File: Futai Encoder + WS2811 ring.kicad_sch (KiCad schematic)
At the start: 42 parts, among them J1 Conn_02x05_Top_Bottom, SW1 RotaryEncoder_Switch_RGB

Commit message: v0.9
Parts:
- added R51, R61, R71: 15k, Resistor_SMD:R_0805_2012Metric, symbol Device:R_Small
- added R52, R62, R72: 2k, Resistor_SMD:R_0805_2012Metric, symbol Device:R_Small
- added R81: 100, Resistor_SMD:R_0805_2012Metric, symbol Device:R_Small
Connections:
- net +5VL: now also R81.1; no longer SW1.1 (C+)
- net BLU: now also R71.1, R72.2; no longer J1.8 (Pin_8)
- net GND: now also R52.1, R62.1, R72.1
- net GRE: now also R61.1, R62.2; no longer J1.7 (Pin_7)
- net RED: now also R51.1, R52.2; no longer J1.6 (Pin_6)
- new net: R81.2, SW1.1 (C+)
- new net Q-BLU: J1.8 (Pin_8), R71.2
- new net Q-GRE: J1.7 (Pin_7), R61.2
- new net Q-RED: J1.6 (Pin_6), R51.2
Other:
- note added: "V deviders for encoder LED ** 24V PWM in expected !**"
- moved on the sheet: C1, C11, C21, C3, C31, C41, C5, C7, C9, D1, D10, D11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

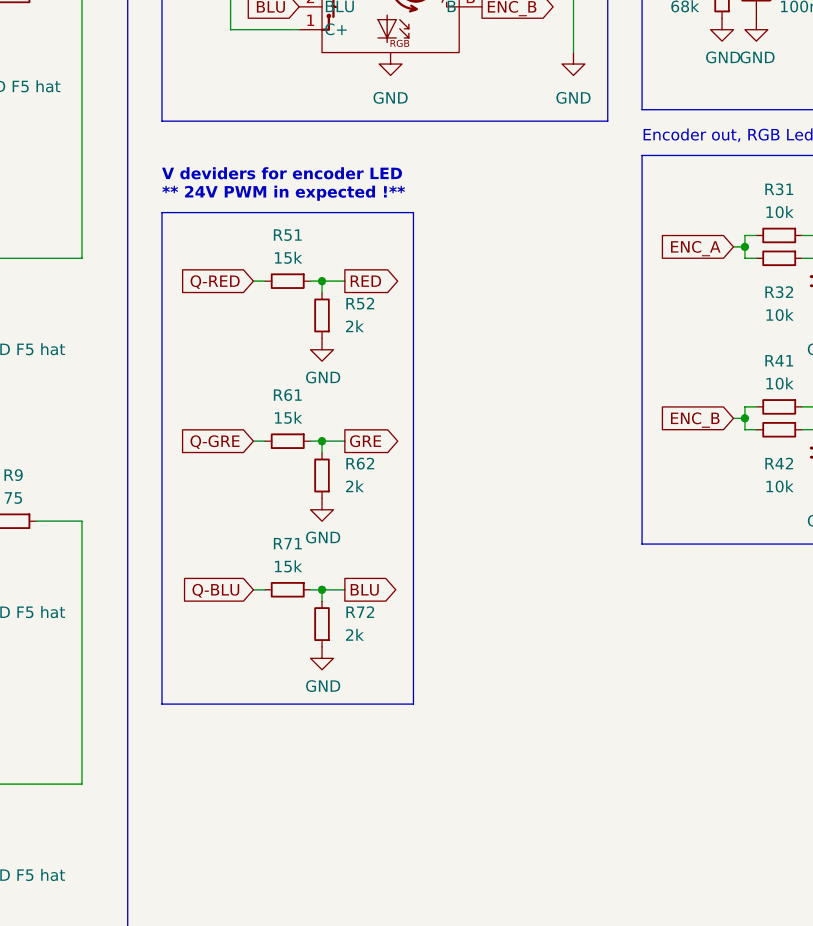
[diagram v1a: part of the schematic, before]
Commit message: better edge cut, adding more info to README.md
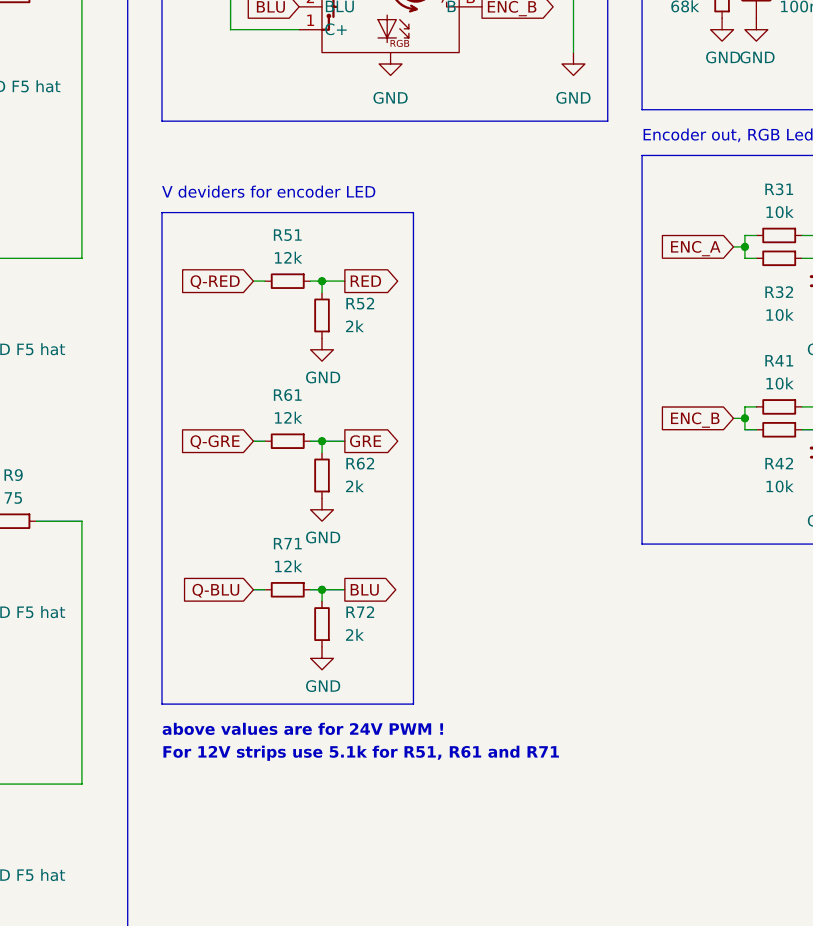
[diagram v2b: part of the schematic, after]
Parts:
- R51, R61, R71: value 15k -> 12k
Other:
- note added: "For 12V strips use 5.1k for R51, R61 and R71"
- note added: "V deviders for encoder LED"
- note added: "above values are for 24V PWM !"
- note removed: "V deviders for encoder LED ** 24V PWM in expected !**"
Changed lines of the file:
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@@
     (stroke (width 0) (type default) (color 0 0 0 0))
+  )
+  (text "For 12V strips use 5.1k for R51, R61 and R71" (at 130.81 134.62 0)
+    (effects (font (size 1.27 1.27) (thickness 0.254) bold) (justify left bottom))
   )
   (text "LED ring" (at 40.64 30.48 0)
@@
     (effects (font (size 1.27 1.27)) (justify left bottom))
   )
+  (text "above values are for 24V PWM !" (at 130.81 132.08 0)
+    (effects (font (size 1.27 1.27) (thickness 0.254) bold) (justify left bottom))
+  )
   (text "Encoder out, RGB Led" (at 184.15 66.04 0)
     (effects (font (size 1.27 1.27)) (justify left bottom))
   )
-  (text "V deviders for encoder LED\n** 24V PWM in expected !**"
-    (at 130.81 72.39 0)
-    (effects (font (size 1.27 1.27) (thickness 0.254) bold) (justify left bottom))
+  (text "V deviders for encoder LED" (at 130.81 72.39 0)
+    (effects (font (size 1.27 1.27)) (justify left bottom))
   )
   (text "Connector interface" (at 274.32 57.15 180)
@@
     (in_bom yes) (on_board yes)
     (property "Reference" "R51" (id 0) (at 144.78 76.2 90))
-    (property "Value" "15k" (id 1) (at 144.78 78.74 90))
+    (property "Value" "12k" (id 1) (at 144.78 78.74 90))
     (property "Footprint" "Resistor_SMD:R_0805_2012Metric" (id 2) (at 144.78 81.28 0)
       (effects (font (size 1.27 1.27)) hide)
@@
     (in_bom yes) (on_board yes)
     (property "Reference" "R61" (id 0) (at 144.78 93.98 90))
-    (property "Value" "15k" (id 1) (at 144.78 96.52 90))
+    (property "Value" "12k" (id 1) (at 144.78 96.52 90))
     (property "Footprint" "Resistor_SMD:R_0805_2012Metric" (id 2) (at 144.78 99.06 0)
       (effects (font (size 1.27 1.27)) hide)
@@
     (in_bom yes) (on_board yes)
     (property "Reference" "R71" (id 0) (at 144.78 110.49 90))
-    (property "Value" "15k" (id 1) (at 144.78 113.03 90))
+    (property "Value" "12k" (id 1) (at 144.78 113.03 90))
     (property "Footprint" "Resistor_SMD:R_0805_2012Metric" (id 2) (at 144.78 115.57 0)
       (effects (font (size 1.27 1.27)) hide)
@@
     )
     (path "/6ff9b25c-f418-4cf8-b38f-8f8fe318f037"
-      (reference "R51") (unit 1) (value "15k") (footprint "Resistor_SMD:R_0805_2012Metric")
+      (reference "R51") (unit 1) (value "12k") (footprint "Resistor_SMD:R_0805_2012Metric")
     )
     (path "/875bf8bf-ec74-4bfd-89a5-45076164d4fd"
@@
     )
     (path "/a1e6e2c4-397e-4467-9a6c-eb9cdfe26fd1"
-      (reference "R61") (unit 1) (value "15k") (footprint "Resistor_SMD:R_0805_2012Metric")
+      (reference "R61") (unit 1) (value "12k") (footprint "Resistor_SMD:R_0805_2012Metric")
     )
     (path "/6929fa9d-4d05-4176-9dd5-104782e2c2d2"
@@
     )
     (path "/b4ca32b1-4944-487b-bee5-cfd3eb8235c2"
-      (reference "R71") (unit 1) (value "15k") (footprint "Resistor_SMD:R_0805_2012Metric")
+      (reference "R71") (unit 1) (value "12k") (footprint "Resistor_SMD:R_0805_2012Metric")
     )
     (path "/a5049ba0-bab0-4b7f-bf3e-59447638b0f9"

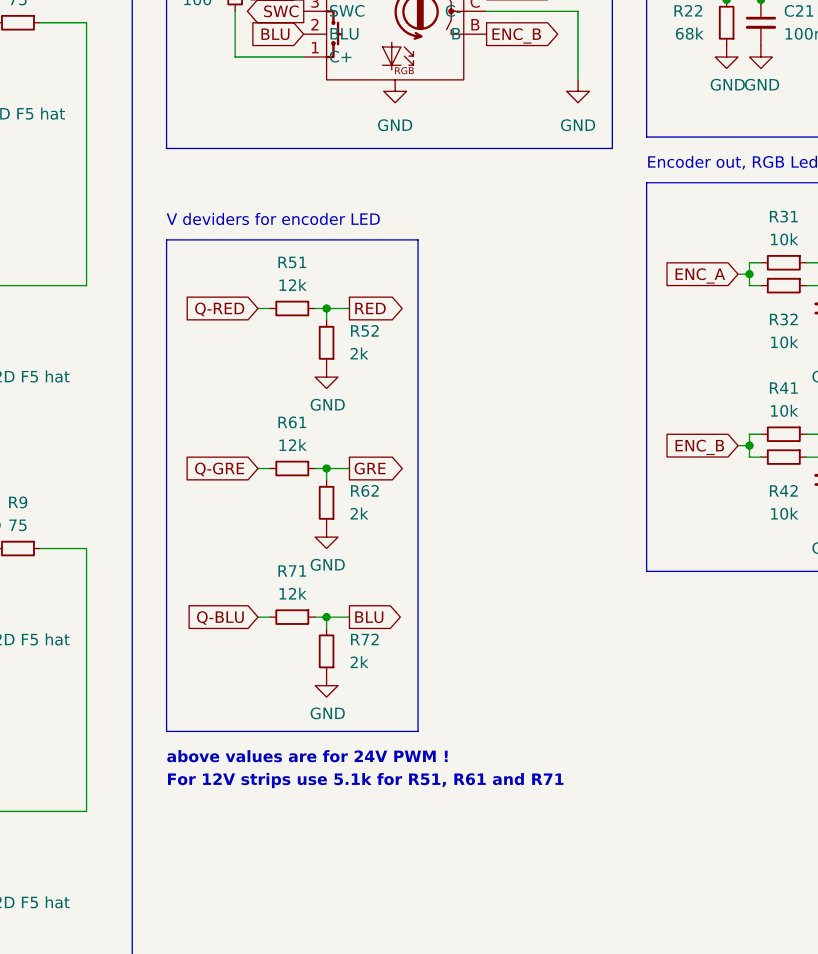
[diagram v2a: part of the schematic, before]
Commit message: encoder with shorter handle
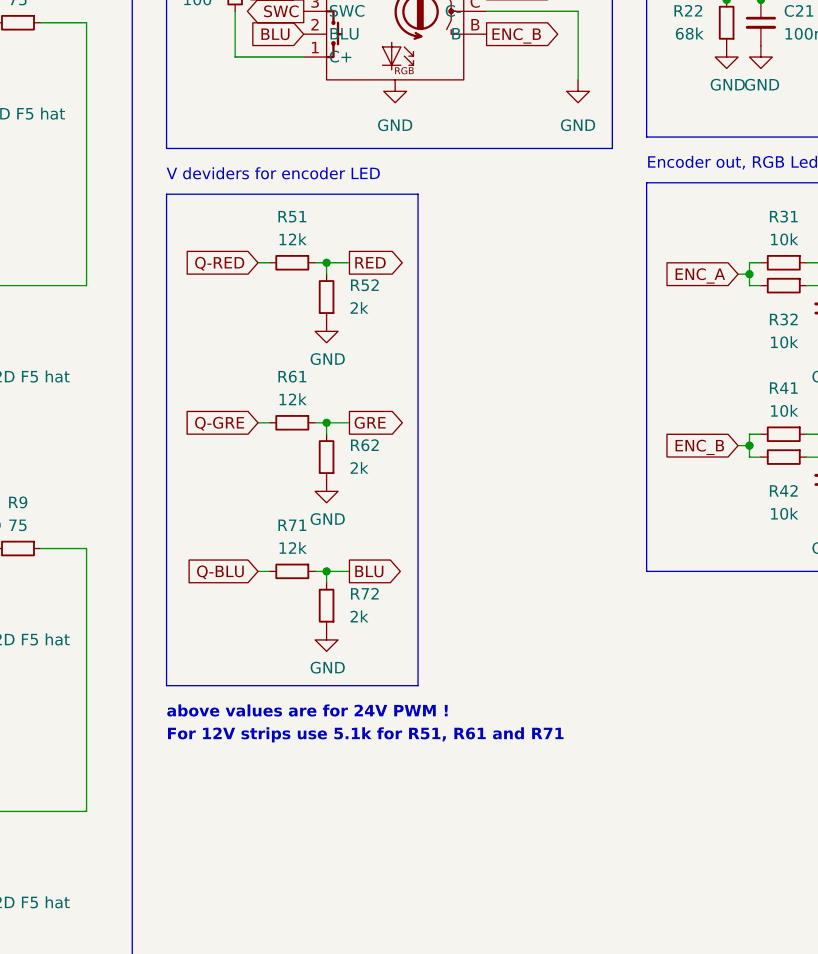
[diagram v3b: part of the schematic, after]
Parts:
- SW1: Purchase https://www.aliexpress.com/item/1005002478234416.html -> https://www.aliexpress.com/item/1005002478550056.html
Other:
- moved on the sheet: R51, R52, R61, R62, R71, R72

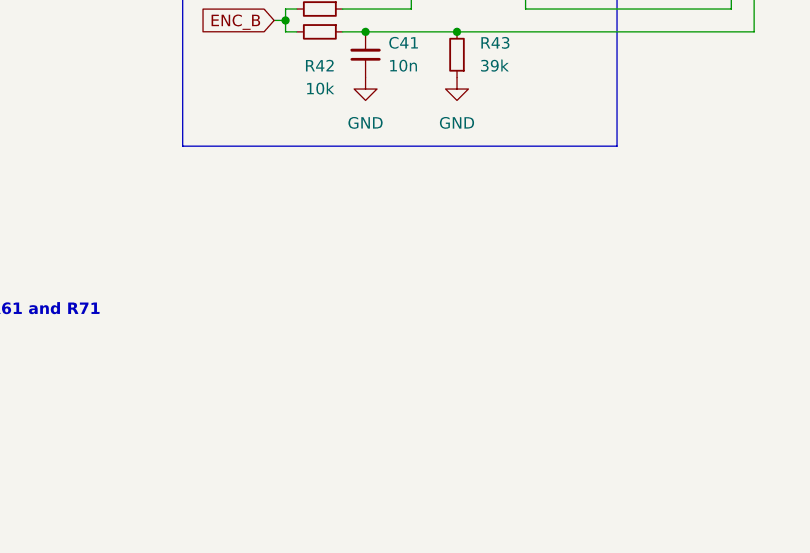
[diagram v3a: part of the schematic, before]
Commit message: adding M3 hole beneth encoder to mark drill hole on panel
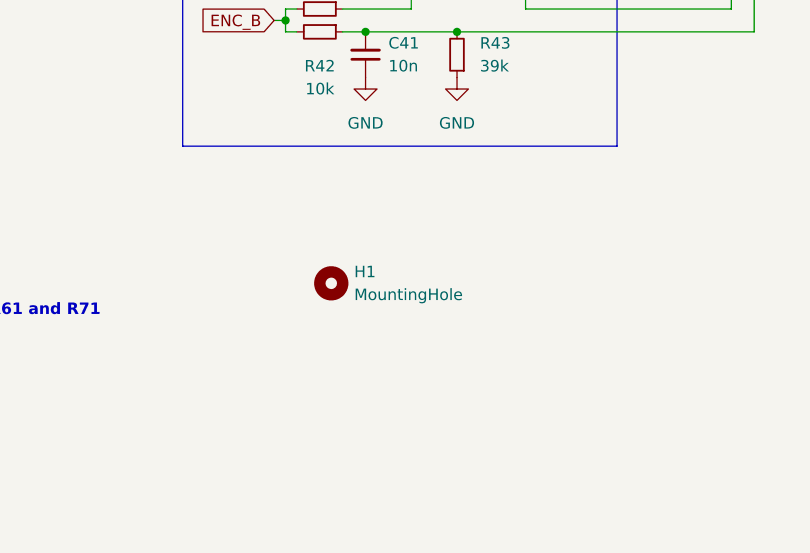
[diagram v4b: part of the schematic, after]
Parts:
- added H1: MountingHole, andilge KiCad footprints:MountingHole_3.2mm_M3, symbol Mechanical:MountingHole
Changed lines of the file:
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@@
   (title_block
     (title "enlighted rotary encoder")
-    (date "2022-01-20")
-    (rev "0.8")
+    (date "2022-01-31")
+    (rev "0.85")
     (company "designed by andilge")
   )
@@
     (pin "1")
     (pin "2")
+  )
+  (symbol (lib_id "Mechanical:MountingHole") (at 200.66 125.73 0) (unit 1)
+    (in_bom yes) (on_board yes) (fields_autoplaced)
+    (property "Reference" "H1" (id 0) (at 203.2 124.4599 0)
+      (effects (font (size 1.27 1.27)) (justify left))
+    )
+    (property "Value" "MountingHole" (id 1) (at 203.2 126.9999 0)
+      (effects (font (size 1.27 1.27)) (justify left))
+    )
+    (property "Footprint" "andilge KiCad footprints:MountingHole_3.2mm_M3" (id 2) (at 200.66 125.73 0)
+      (effects (font (size 1.27 1.27)) hide)
+    )
+    (property "Datasheet" "~" (id 3) (at 200.66 125.73 0)
+      (effects (font (size 1.27 1.27)) hide)
+    )
   )
   (symbol (lib_id "Device:R_Small") (at 114.3 49.53 270) (unit 1)
@@
       (reference "D12") (unit 1) (value "WS2812D F5 hat") (footprint "andilge KiCad footprints:WS2811D-F5-1261")
     )
+    (path "/612dc420-c0a9-4dad-8f27-8ff7c0ae1729"
+      (reference "H1") (unit 1) (value "MountingHole") (footprint "andilge KiCad footprints:MountingHole_3.2mm_M3")
+    )
     (path "/d71593f7-09cf-4465-9cce-fd2751f1f4fa"

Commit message: brushing up schematic diagram.pdf
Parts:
- added R12: 75Ω, Resistor_SMD:R_0805_2012Metric, symbol Device:R_Small
- C1, C11, C3, C5, C7, C9: value 220n -> 220nF
- C21: value 100n -> 100nF
- C31, C41: value 10n -> 10nF
- R1, R10, R11, R2, R3, R4, R5, R6, R7, R8, R9: value 75 -> 75Ω
- R21: value 33k -> 33kΩ
- R22: value 68k -> 68kΩ
- R31, R32, R41, R42: value 10k -> 10kΩ
- R33, R43: value 39k -> 39kΩ
- R51, R61, R71: value 12k -> 12kΩ
- R52, R62, R72: value 2k -> 2kΩ
- R81: value 100 -> 100Ω
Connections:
- net DOUT: now also R12.2; no longer D12.1 (DOUT)
- net at D9.1 (DOUT): now also R9.1; no longer R9.2
- net at D10.4 (DIN): now also R9.2; no longer R9.1
- net at D3.1 (DOUT): now also R3.1; no longer R3.2
- net at D4.4 (DIN): now also R3.2; no longer R3.1
- new net: D12.1 (DOUT), R12.1
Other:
- note added: "Encoder out, RGB Led in"
- note added: "For 12V strips use 5.1kΩ for R51, R61 and R71"
- note added: "Power in, switch out, data in/out"
- note removed: "Encoder out, RGB Led"
- note removed: "For 12V strips use 5.1k for R51, R61 and R71"
- note removed: "Power, switch, data in/out"
- moved on the sheet: C1, C11, C21, C3, C31, C41, C5, C7, C9, D1, D10, D11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

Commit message: fixing typo
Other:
- note added: "V dividers for encoder LED"
- note removed: "V deviders for encoder LED"
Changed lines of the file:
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@@
     (effects (font (size 1.27 1.27)) (justify left bottom))
   )
-  (text "V deviders for encoder LED" (at 127 57.15 0)
+  (text "V dividers for encoder LED" (at 127 57.15 0)
     (effects (font (size 1.27 1.27)) (justify left bottom))
   )

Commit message: smaller center hole
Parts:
- H1: footprint andilge KiCad footprints:MountingHole_3.2mm_M3 -> andilge KiCad footprints:MountingHole_2.2mm_M2
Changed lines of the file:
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@@
       (effects (font (size 1.27 1.27)) (justify left))
     )
-    (property "Footprint" "andilge KiCad footprints:MountingHole_3.2mm_M3" (id 2) (at 194.31 115.57 0)
+    (property "Footprint" "andilge KiCad footprints:MountingHole_2.2mm_M2" (id 2) (at 194.31 115.57 0)
       (effects (font (size 1.27 1.27)) hide)
     )
@@
     )
     (path "/612dc420-c0a9-4dad-8f27-8ff7c0ae1729"
-      (reference "H1") (unit 1) (value "MountingHole") (footprint "andilge KiCad footprints:MountingHole_3.2mm_M3")
+      (reference "H1") (unit 1) (value "MountingHole") (footprint "andilge KiCad footprints:MountingHole_2.2mm_M2")
     )
     (path "/d71593f7-09cf-4465-9cce-fd2751f1f4fa"
